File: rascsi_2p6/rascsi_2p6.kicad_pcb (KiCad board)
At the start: 2 copper layers, 65 x 56 mm, 95 parts, among them IC1 SN74LS641-1DW, IC2 SN74LS641-1DW, IC3 SN74LS641-1DW, IC4 SN74LS641-1DW, J1 Raspberry_Pi_2_3, J2 DNP, J20 171826-4, J3 Conn_02x25_Odd_Even, J4 I2C Pinout, J5 DNP, J6 CONNFLY DB-25, J8 USB_B_Micro, J9 Conn_02x25_Odd_Even, X1 Mac, X2 Dogcow, X3 Mac, X4 Dogcow, X5 Dogcow, X6 Dogcow, X7 Pi, X8 Pi

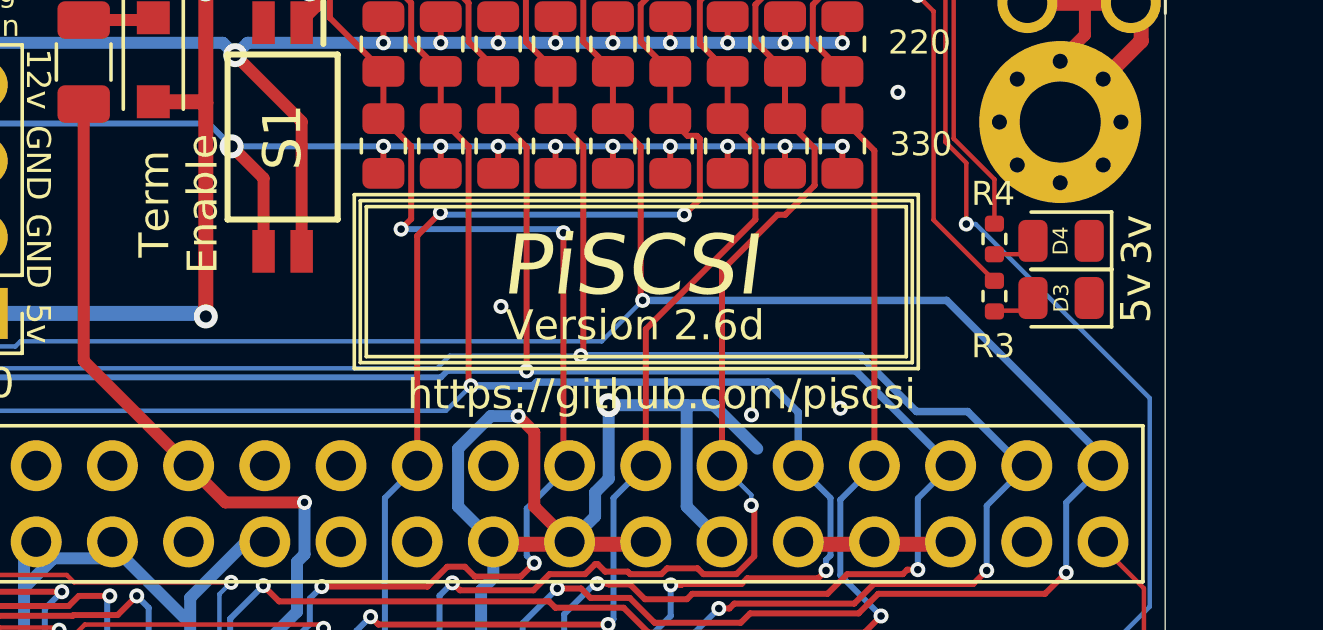
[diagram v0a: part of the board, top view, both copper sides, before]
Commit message: Revert back to original version of rascsi 2.6 board.
This reverts commit 2b424468fa236e169660193e1614c490b0ff0ed6.
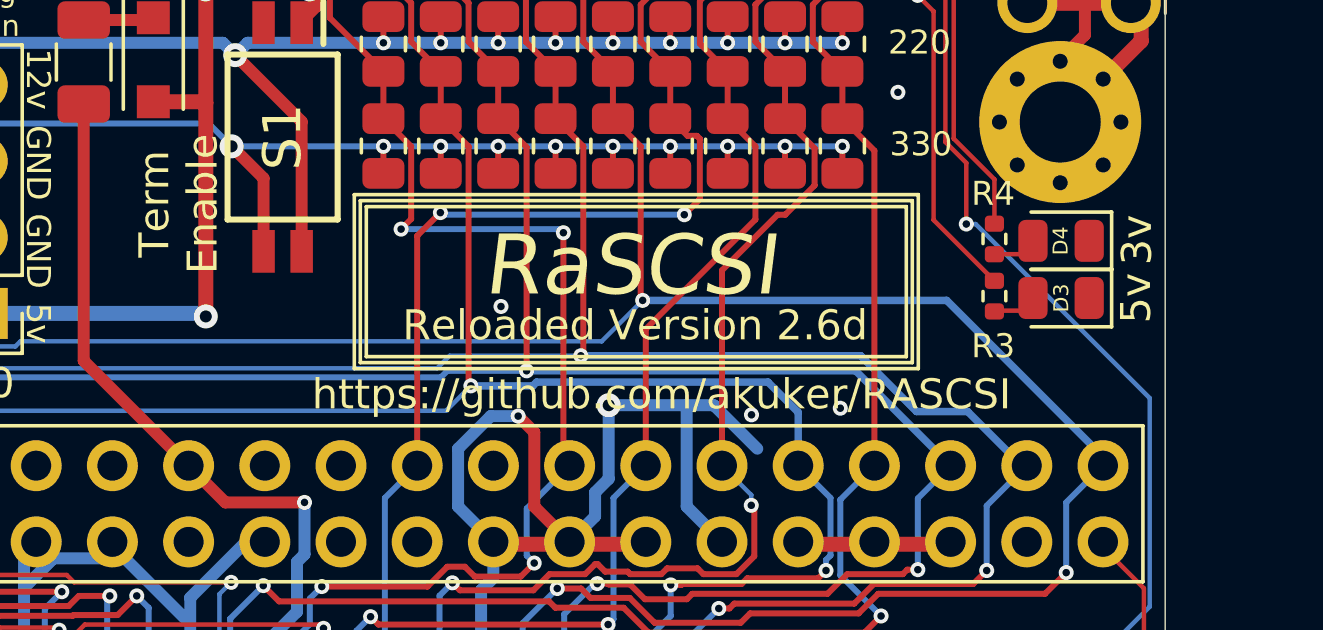
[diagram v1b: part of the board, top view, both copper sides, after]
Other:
- board text added: "RaSCSI"
- board text added: "Reloaded Version 2.6d"
- board text added: "https://github.com/akuker/RASCSI"
- board text removed: "PiSCSI"
- board text removed: "Version 2.6d"
- board text removed: "https://github.com/piscsi"
- board text removed: "https://github.com/piscsi Copyright 2022 akuker"
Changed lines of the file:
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@@
     (property "Sheetfile" "rascsi_2p6.kicad_sch")
     (property "Sheetname" "")
-    (attr through_hole exclude_from_pos_files exclude_from_bom)
+    (attr through_hole)
     (fp_text reference "X2" (at 0.25 4.5) (layer "Cmts.User") hide
       (effects (font (size 1.524 1.524) (thickness 0.3)))
@@
     (property "Sheetfile" "rascsi_2p6.kicad_sch")
     (property "Sheetname" "")
-    (attr through_hole exclude_from_pos_files exclude_from_bom)
+    (attr through_hole)
     (fp_text reference "X4" (at 0.25 4.5) (layer "F.SilkS") hide
       (effects (font (size 1.524 1.524) (thickness 0.3)))
@@
     (property "Sheetfile" "rascsi_2p6.kicad_sch")
     (property "Sheetname" "")
-    (attr through_hole exclude_from_pos_files exclude_from_bom)
+    (attr through_hole)
     (fp_text reference "X5" (at 0.25 4.5) (layer "Cmts.User") hide
       (effects (font (size 1.524 1.524) (thickness 0.3)))
@@
     (property "Sheetfile" "rascsi_2p6.kicad_sch")
     (property "Sheetname" "")
-    (attr through_hole exclude_from_pos_files exclude_from_bom)
+    (attr through_hole)
     (fp_text reference "X6" (at 0.25 4.5) (layer "F.SilkS") hide
       (effects (font (size 1.524 1.524) (thickness 0.3)))
@@
     (property "Sheetfile" "rascsi_2p6.kicad_sch")
     (property "Sheetname" "")
-    (attr through_hole exclude_from_pos_files exclude_from_bom)
+    (attr through_hole)
     (fp_text reference "X1" (at 0 0) (layer "F.SilkS") hide
       (effects (font (size 1.524 1.524) (thickness 0.3)))
@@
     (property "Sheetfile" "Connectors.kicad_sch")
     (property "Sheetname" "Connectors")
-    (attr through_hole exclude_from_pos_files exclude_from_bom)
+    (attr through_hole)
     (fp_text reference "J9" (at 4.1 -2 -90) (layer "F.SilkS") hide
       (effects (font (size 1 1) (thickness 0.15)))
@@
     (tags "Through hole socket strip THT 2x20 2.54mm double row")
     (property "Description" "Female Header 40 2 right-angle，180degrees 2.54mm 2.54mm Pin Header & Female Header RoHS")
-    (property "LCSC" "C169819")
+    (property "LCSC" "C50982")
     (property "Manufacturer_Name" "BOOMELE(Boom Precision Elec)")
     (property "Manufacturer_Part_Number" "C50982")
@@
     (property "Sheetfile" "rascsi_2p6.kicad_sch")
     (property "Sheetname" "")
-    (attr through_hole exclude_from_pos_files exclude_from_bom)
+    (attr through_hole)
     (fp_text reference "X7" (at 0 0) (layer "Cmts.User") hide
       (effects (font (size 1.524 1.524) (thickness 0.3)))
@@
     (property "Sheetfile" "rascsi_2p6.kicad_sch")
     (property "Sheetname" "")
-    (attr through_hole exclude_from_pos_files exclude_from_bom)
+    (attr through_hole)
     (fp_text reference "X3" (at 0.0635 -0.127) (layer "Cmts.User") hide
       (effects (font (size 1.524 1.524) (thickness 0.3)))
@@
     (property "Sheetfile" "rascsi_2p6.kicad_sch")
     (property "Sheetname" "")
-    (attr through_hole exclude_from_pos_files exclude_from_bom)
+    (attr through_hole)
     (fp_text reference "X8" (at -2.56 2.6) (layer "Cmts.User") hide
       (effects (font (size 1.524 1.524) (thickness 0.3)))
@@
     (effects (font (size 0.8 0.8) (thickness 0.15)) (justify mirror))
   )
-  (gr_text "Version 2.6d" (at 205.06 57.7) (layer "B.SilkS")
+  (gr_text "Reloaded Version 2.6d" (at 205.06 57.7) (layer "B.SilkS")
     (effects (font (size 1 1) (thickness 0.15)) (justify mirror))
   )
@@
     (effects (font (size 0.8 0.8) (thickness 0.15)) (justify mirror))
   )
-  (gr_text "https://github.com/piscsi\nCopyright 2022 akuker" (at 204.97 62.75) (layer "B.SilkS")
+  (gr_text "https://github.com/akuker/RASCSI" (at 204.97 62.09) (layer "B.SilkS")
     (effects (font (size 1 1) (thickness 0.15)) (justify mirror))
   )
@@
     (effects (font (size 1 1) (thickness 0.15)) (justify mirror))
   )
-  (gr_text "PiSCSI" (at 205.22 55.71) (layer "B.SilkS")
+  (gr_text "RaSCSI" (at 205.22 55.71) (layer "B.SilkS")
     (effects (font (size 2 2) (thickness 0.4) italic) (justify mirror))
   )
@@
     (effects (font (size 1 1) (thickness 0.15)))
   )
-  (gr_text "https://github.com/piscsi" (at 222.71 78.08) (layer "F.SilkS")
+  (gr_text "https://github.com/akuker/RASCSI" (at 222.71 78.08) (layer "F.SilkS")
     (effects (font (size 1 1) (thickness 0.15)))
   )
@@
     (effects (font (size 0.8 0.8) (thickness 0.15)))
   )
-  (gr_text "PiSCSI" (at 221.67 73.79) (layer "F.SilkS")
+  (gr_text "RaSCSI" (at 221.67 73.79) (layer "F.SilkS")
     (effects (font (size 2 2) (thickness 0.4) italic))
   )
@@
     (effects (font (size 1 1) (thickness 0.15)))
   )
-  (gr_text "Version 2.6d" (at 221.83 75.78) (layer "F.SilkS")
+  (gr_text "Reloaded Version 2.6d" (at 221.83 75.78) (layer "F.SilkS")
     (effects (font (size 1 1) (thickness 0.15)))
   )

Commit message: update silkscreen to say piscsi and regenerate prod files
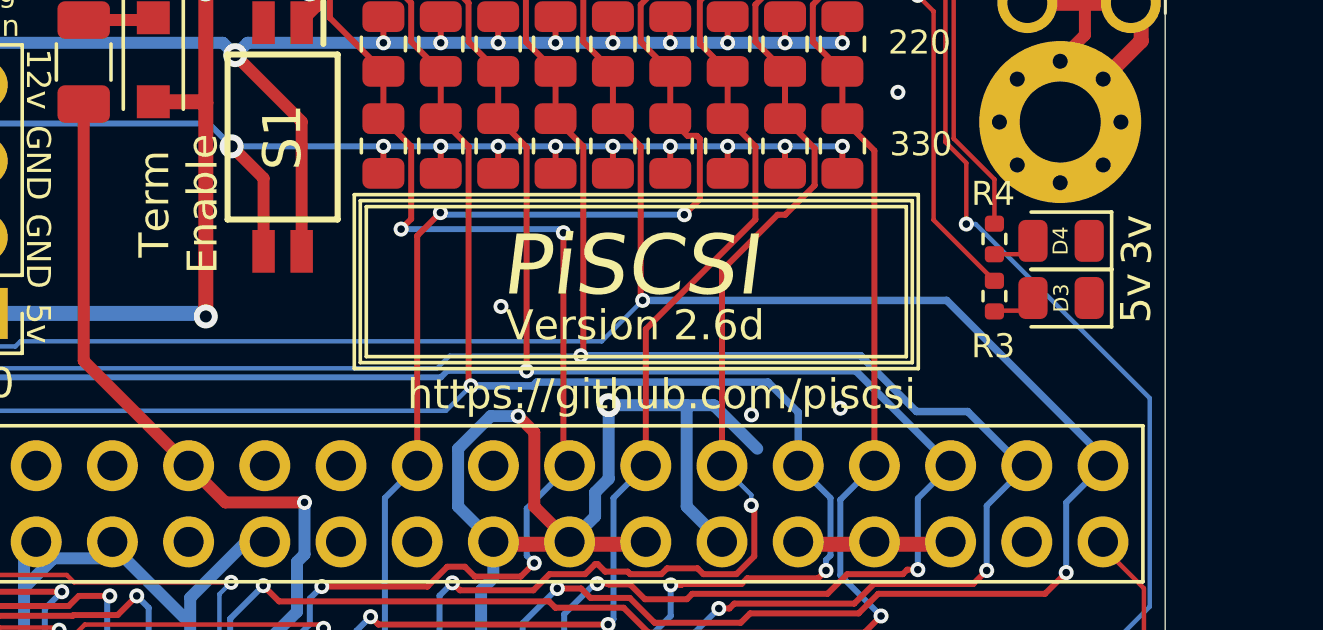
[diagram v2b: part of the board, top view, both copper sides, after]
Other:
- board text added: "PiSCSI"
- board text added: "Version 2.6d"
- board text added: "https://github.com/piscsi"
- board text added: "https://github.com/piscsi Copyright 2022 akuker"
- board text removed: "RaSCSI"
- board text removed: "Reloaded Version 2.6d"
- board text removed: "https://github.com/akuker/RASCSI"
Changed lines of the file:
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@@
     (property "Sheetfile" "rascsi_2p6.kicad_sch")
     (property "Sheetname" "")
-    (attr through_hole)
+    (attr through_hole exclude_from_pos_files exclude_from_bom)
     (fp_text reference "X2" (at 0.25 4.5) (layer "Cmts.User") hide
       (effects (font (size 1.524 1.524) (thickness 0.3)))
@@
     (property "Sheetfile" "rascsi_2p6.kicad_sch")
     (property "Sheetname" "")
-    (attr through_hole)
+    (attr through_hole exclude_from_pos_files exclude_from_bom)
     (fp_text reference "X4" (at 0.25 4.5) (layer "F.SilkS") hide
       (effects (font (size 1.524 1.524) (thickness 0.3)))
@@
     (property "Sheetfile" "rascsi_2p6.kicad_sch")
     (property "Sheetname" "")
-    (attr through_hole)
+    (attr through_hole exclude_from_pos_files exclude_from_bom)
     (fp_text reference "X5" (at 0.25 4.5) (layer "Cmts.User") hide
       (effects (font (size 1.524 1.524) (thickness 0.3)))
@@
     (property "Sheetfile" "rascsi_2p6.kicad_sch")
     (property "Sheetname" "")
-    (attr through_hole)
+    (attr through_hole exclude_from_pos_files exclude_from_bom)
     (fp_text reference "X6" (at 0.25 4.5) (layer "F.SilkS") hide
       (effects (font (size 1.524 1.524) (thickness 0.3)))
@@
     (property "Sheetfile" "rascsi_2p6.kicad_sch")
     (property "Sheetname" "")
-    (attr through_hole)
+    (attr through_hole exclude_from_pos_files exclude_from_bom)
     (fp_text reference "X1" (at 0 0) (layer "F.SilkS") hide
       (effects (font (size 1.524 1.524) (thickness 0.3)))
@@
     (property "Sheetfile" "Connectors.kicad_sch")
     (property "Sheetname" "Connectors")
-    (attr through_hole)
+    (attr through_hole exclude_from_pos_files exclude_from_bom)
     (fp_text reference "J9" (at 4.1 -2 -90) (layer "F.SilkS") hide
       (effects (font (size 1 1) (thickness 0.15)))
@@
     (tags "Through hole socket strip THT 2x20 2.54mm double row")
     (property "Description" "Female Header 40 2 right-angle，180degrees 2.54mm 2.54mm Pin Header & Female Header RoHS")
-    (property "LCSC" "C50982")
+    (property "LCSC" "C169819")
     (property "Manufacturer_Name" "BOOMELE(Boom Precision Elec)")
     (property "Manufacturer_Part_Number" "C50982")
@@
     (property "Sheetfile" "rascsi_2p6.kicad_sch")
     (property "Sheetname" "")
-    (attr through_hole)
+    (attr through_hole exclude_from_pos_files exclude_from_bom)
     (fp_text reference "X7" (at 0 0) (layer "Cmts.User") hide
       (effects (font (size 1.524 1.524) (thickness 0.3)))
@@
     (property "Sheetfile" "rascsi_2p6.kicad_sch")
     (property "Sheetname" "")
-    (attr through_hole)
+    (attr through_hole exclude_from_pos_files exclude_from_bom)
     (fp_text reference "X3" (at 0.0635 -0.127) (layer "Cmts.User") hide
       (effects (font (size 1.524 1.524) (thickness 0.3)))
@@
     (property "Sheetfile" "rascsi_2p6.kicad_sch")
     (property "Sheetname" "")
-    (attr through_hole)
+    (attr through_hole exclude_from_pos_files exclude_from_bom)
     (fp_text reference "X8" (at -2.56 2.6) (layer "Cmts.User") hide
       (effects (font (size 1.524 1.524) (thickness 0.3)))
@@
     (effects (font (size 0.8 0.8) (thickness 0.15)) (justify mirror))
   )
-  (gr_text "Reloaded Version 2.6d" (at 205.06 57.7) (layer "B.SilkS")
+  (gr_text "Version 2.6d" (at 205.06 57.7) (layer "B.SilkS")
     (effects (font (size 1 1) (thickness 0.15)) (justify mirror))
   )
@@
     (effects (font (size 0.8 0.8) (thickness 0.15)) (justify mirror))
   )
-  (gr_text "https://github.com/akuker/RASCSI" (at 204.97 62.09) (layer "B.SilkS")
+  (gr_text "https://github.com/piscsi\nCopyright 2022 akuker" (at 204.97 62.75) (layer "B.SilkS")
     (effects (font (size 1 1) (thickness 0.15)) (justify mirror))
   )
@@
     (effects (font (size 1 1) (thickness 0.15)) (justify mirror))
   )
-  (gr_text "RaSCSI" (at 205.22 55.71) (layer "B.SilkS")
+  (gr_text "PiSCSI" (at 205.22 55.71) (layer "B.SilkS")
     (effects (font (size 2 2) (thickness 0.4) italic) (justify mirror))
   )
@@
     (effects (font (size 1 1) (thickness 0.15)))
   )
-  (gr_text "https://github.com/akuker/RASCSI" (at 222.71 78.08) (layer "F.SilkS")
+  (gr_text "https://github.com/piscsi" (at 222.71 78.08) (layer "F.SilkS")
     (effects (font (size 1 1) (thickness 0.15)))
   )
@@
     (effects (font (size 0.8 0.8) (thickness 0.15)))
   )
-  (gr_text "RaSCSI" (at 221.67 73.79) (layer "F.SilkS")
+  (gr_text "PiSCSI" (at 221.67 73.79) (layer "F.SilkS")
     (effects (font (size 2 2) (thickness 0.4) italic))
   )
@@
     (effects (font (size 1 1) (thickness 0.15)))
   )
-  (gr_text "Reloaded Version 2.6d" (at 221.83 75.78) (layer "F.SilkS")
+  (gr_text "Version 2.6d" (at 221.83 75.78) (layer "F.SilkS")
     (effects (font (size 1 1) (thickness 0.15)))
   )
